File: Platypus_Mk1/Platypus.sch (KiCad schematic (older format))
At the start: 22 parts, among them CN1 SERVO_PWM, J1 PJ-202AH, J15 12V_TERM, J2 TermLaser, J3 TermStop, J4 LASER_PWR, J5 LASER_PULSE, J6 TermControl, J7 TermLimit, J8 TermAux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

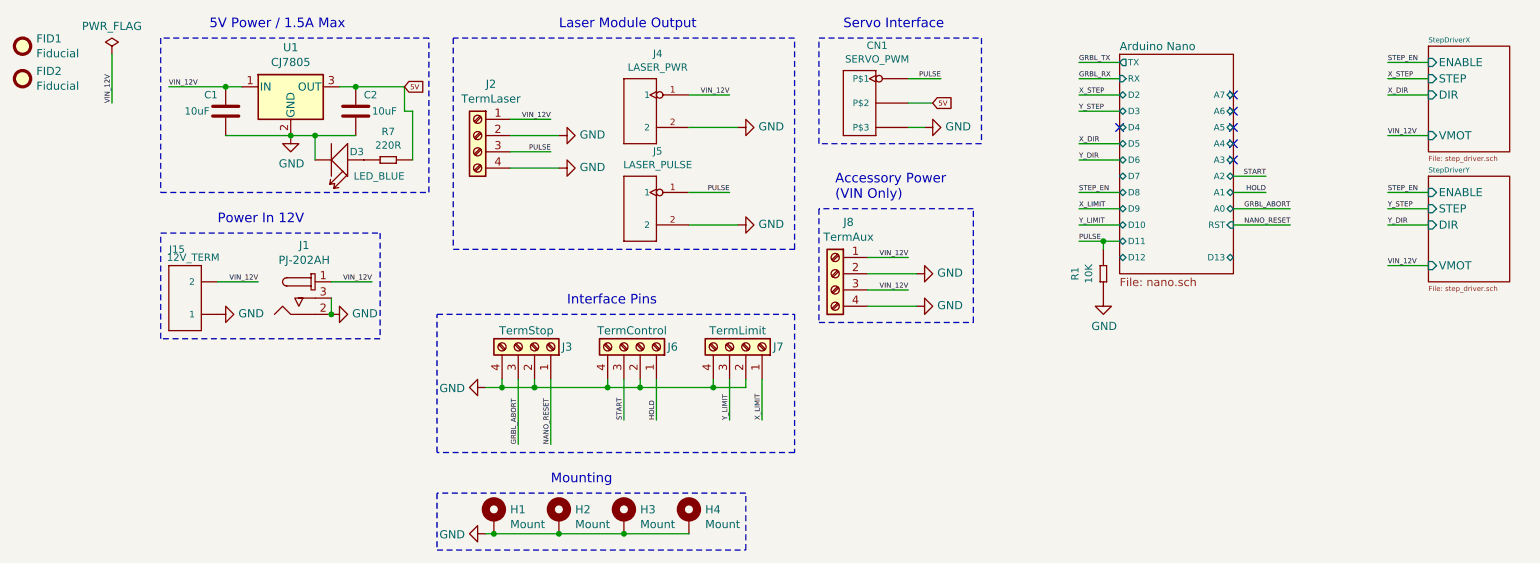
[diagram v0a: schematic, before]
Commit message: Change RX/TX LEDs. Add new laser conn
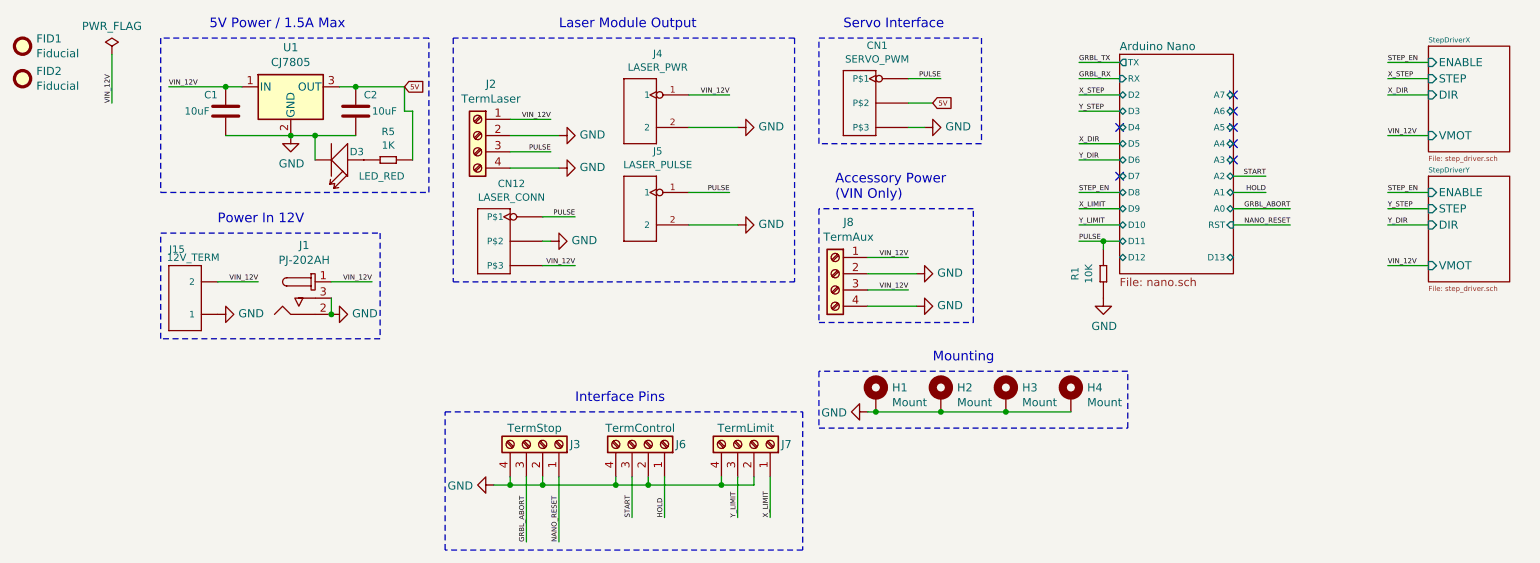
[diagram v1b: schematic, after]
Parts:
- added CN12: LASER_CONN, OPL_Connector:H3-2.54, symbol OPL_Connector:DIP-BLACK-MALE-HEADER-VERT_3P-2.54_
- D3: value LED_BLUE -> LED_RED; MPN 19-217-BHC-ZL1M2RY-3T -> 19-217-R6C-AL1M2VY-3T; SKU 304090045 -> 304090042
- R5: renamed from R7; value 220R -> 1K; MPN RC0603JR-07220RL -> RC0603FR-071KL; SKU 301010163 -> 301010298
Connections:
- net GND: now also CN12.2 (P$2)
- net PULSE: now also CN12.1 (P$1)
- net VIN_12V: now also CN12.3 (P$3)
- no-connect marks 6 -> 7
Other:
- moved on the sheet: H1, H2, H3, H4, J3, J6, J7

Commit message: rework for component moves
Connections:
- net 5V: now also J2.1 (Pin_1), J8.1 (Pin_1)
- net GND: now also J2.3 (Pin_3); no longer J2.2 (Pin_2), J2.4 (Pin_4)
- net PULSE: now also J2.2 (Pin_2); no longer J2.3 (Pin_3)
- net VIN_12V: now also J2.4 (Pin_4); no longer J2.1 (Pin_1), J8.1 (Pin_1)
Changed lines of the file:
@@
 	-1   0    0    -1
 $EndComp
-Text Label 6350 3850 2    31   ~ 0
-VIN_12V
 Text Label 6350 4050 2    31   ~ 0
 VIN_12V
@@
 	1    0    0    -1
 $EndComp
-Text Label 4150 3000 2    31   ~ 0
+Text Label 4150 3300 2    31   ~ 0
 VIN_12V
 $Comp
 L power:GND #PWR04
 U 1 1 5D4DF272
-P 4200 3100
-F 0 "#PWR04" H 4200 2850 50  0001 C CNN
-F 1 "GND" V 4205 2972 50  0000 R CNN
-F 2 "" H 4200 3100 50  0001 C CNN
-F 3 "" H 4200 3100 50  0001 C CNN
-	1    4200 3100
-	0    -1   -1   0
-$EndComp
-$Comp
-L power:GND #PWR05
-U 1 1 5D4DF278
-P 4200 3300
-F 0 "#PWR05" H 4200 3050 50  0001 C CNN
-F 1 "GND" V 4205 3172 50  0000 R CNN
-F 2 "" H 4200 3300 50  0001 C CNN
-F 3 "" H 4200 3300 50  0001 C CNN
-	1    4200 3300
+P 4150 3200
+F 0 "#PWR04" H 4150 2950 50  0001 C CNN
+F 1 "GND" V 4155 3072 50  0000 R CNN
+F 2 "" H 4150 3200 50  0001 C CNN
+F 3 "" H 4150 3200 50  0001 C CNN
+	1    4150 3200
 	0    -1   -1   0
 $EndComp
@@
 	3900 3000 4150 3000
 Wire Wire Line
-	4200 3100 3900 3100
-Wire Wire Line
 	3900 3200 4150 3200
-Wire Wire Line
-	4200 3300 3900 3300
-Text Label 4150 3200 2    31   ~ 0
+Text Label 4150 3100 2    31   ~ 0
 PULSE
 Text Notes 5900 3500 0    59   ~ 0
@@
 	5650 2500 5650 4000
 NoConn ~ 7650 3350
+Text GLabel 4150 3000 2    31   Input ~ 0
+5V
+Wire Wire Line
+	3900 3100 4150 3100
+Wire Wire Line
+	4150 3300 3900 3300
+Text GLabel 6350 3850 2    31   Input ~ 0
+5V
 $EndSCHEMATC
